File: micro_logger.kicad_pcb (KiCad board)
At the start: 2 copper layers, 16.8 x 27.4 mm, 26 parts, among them J3 ISP, J4 Conn_01x02, J5 DM3AT-SF-PEJM5, SW2 SW_Push, U1 MIC5205-3.3, U2 MPU-9250, U3 ATMEGA328-AU, Y1 Crystal_GND2

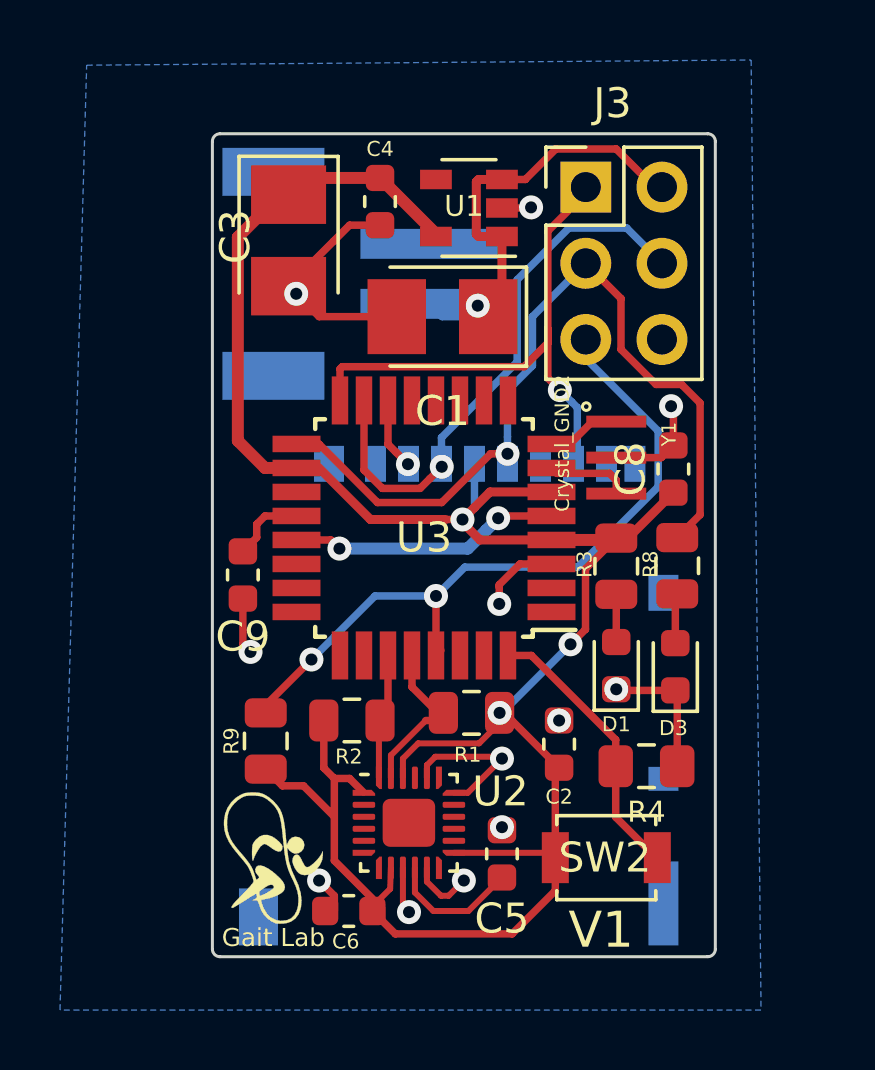
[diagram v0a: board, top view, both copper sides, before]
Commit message: updated layout
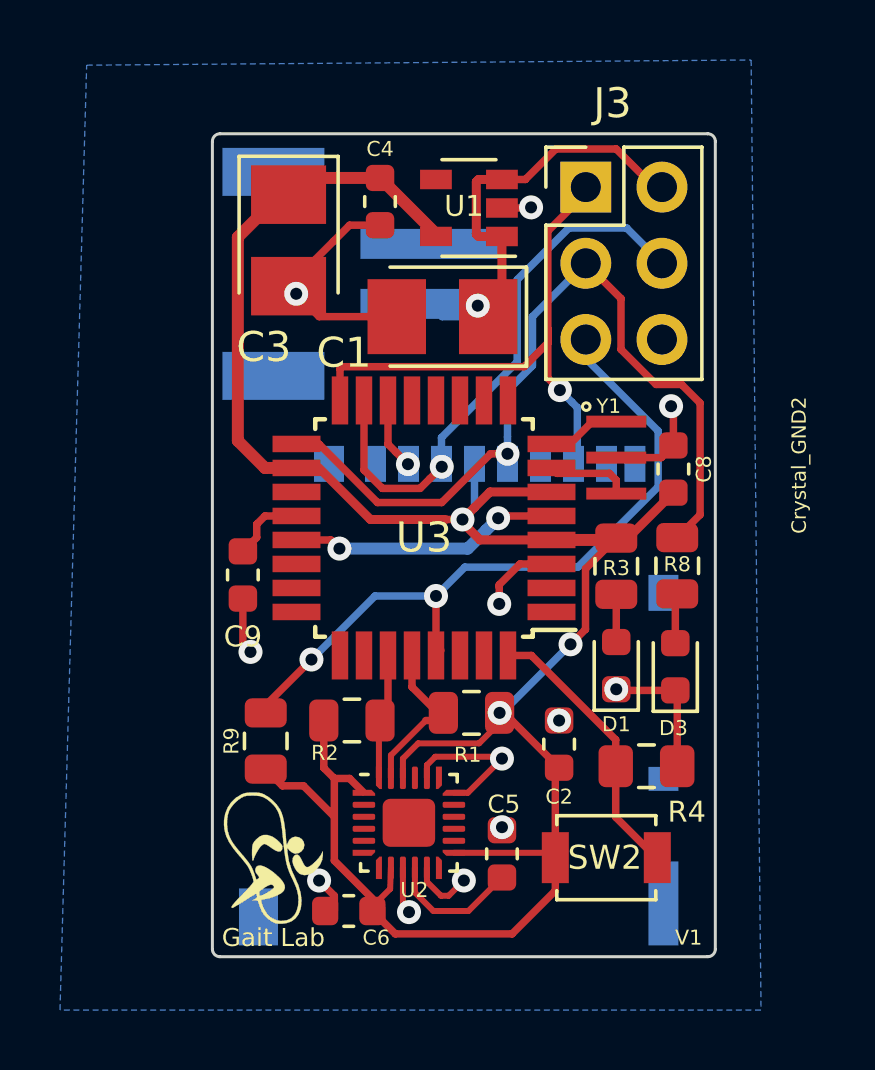
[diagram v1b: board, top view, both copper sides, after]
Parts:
- removed the G*** at (0.00, 0.00)
